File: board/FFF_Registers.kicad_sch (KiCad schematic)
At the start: 19 parts, among them U1 74F573, U14 74F32, U18 74F04, U2 74F541, U47 74F573, U48 74F541, U49 74F573, U50 74F541, U51 74F32, U52 74F04

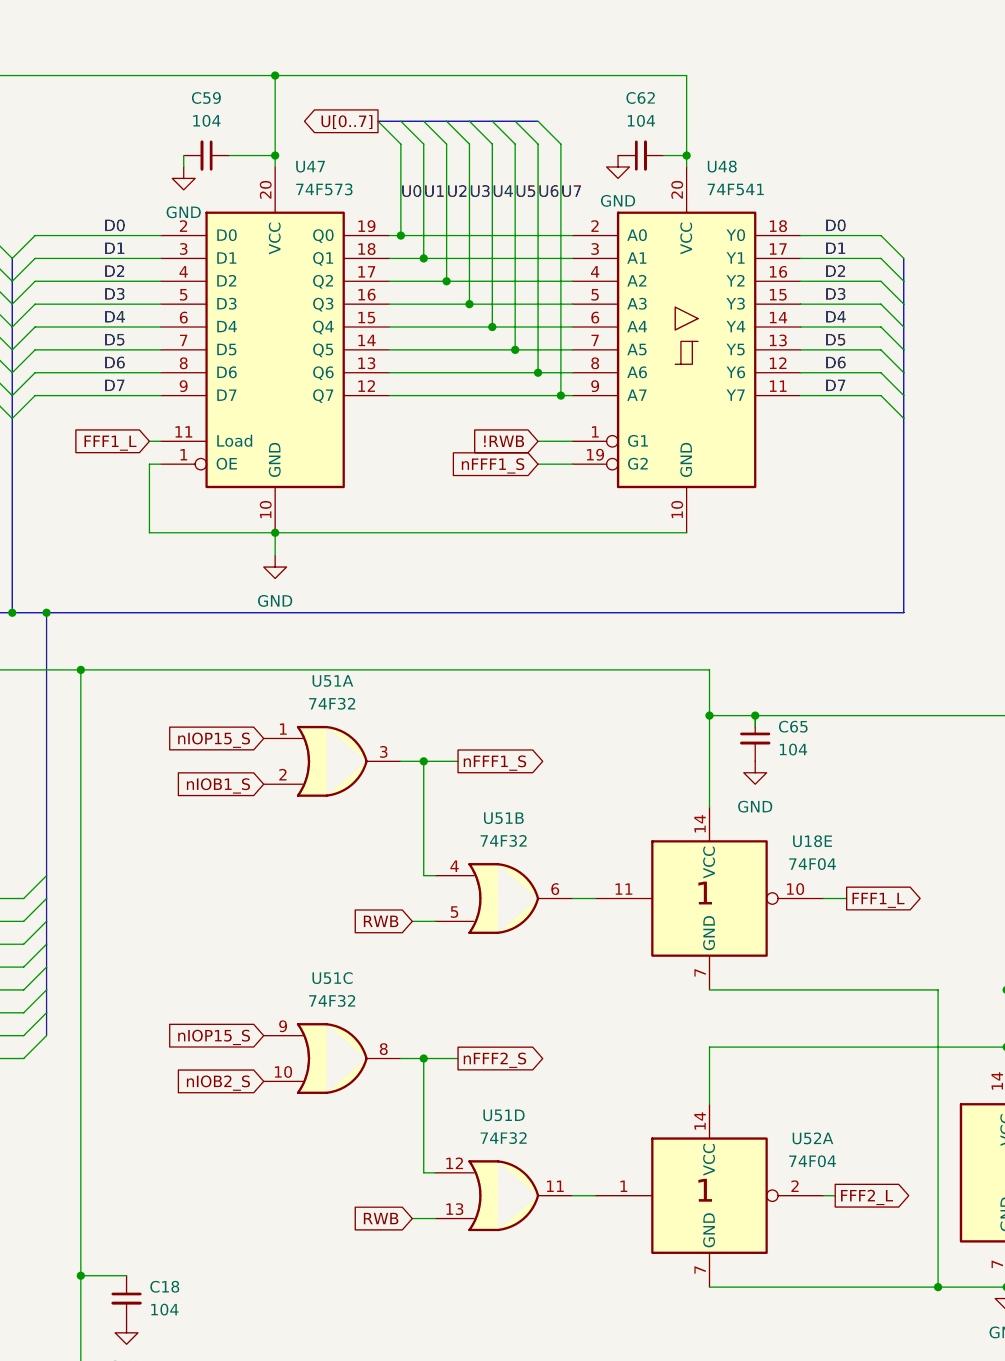
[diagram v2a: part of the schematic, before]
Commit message: Fixing nBROMD routing, removing unnecessary 7404, and minor other cleanup.
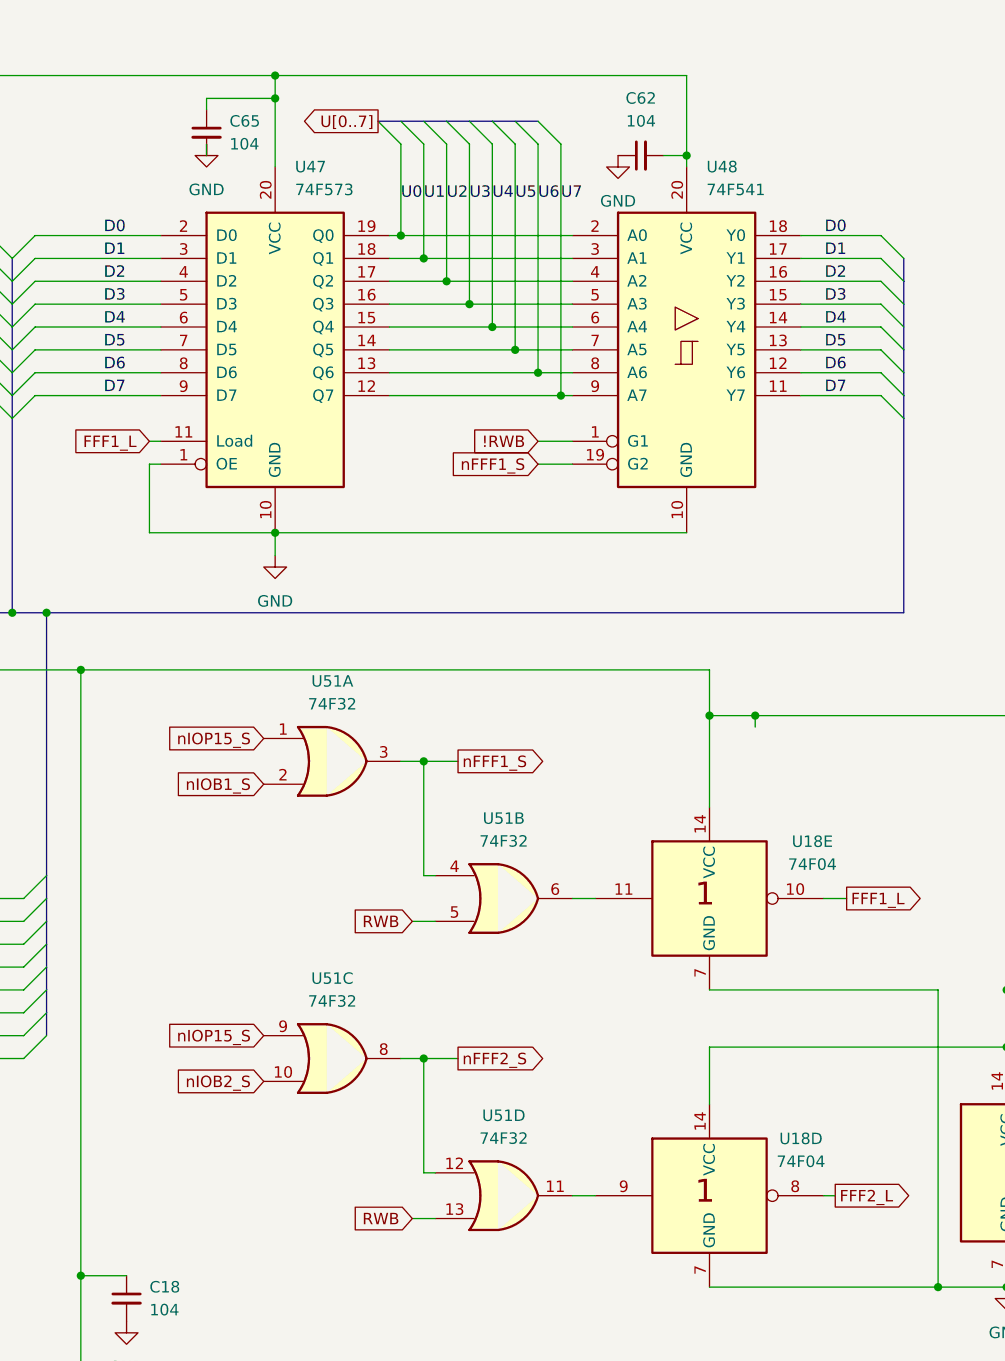
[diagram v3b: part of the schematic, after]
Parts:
- removed C59: 104, Capacitor_THT:C_Disc_D5.0mm_W2.5mm_P5.00mm, symbol Device:C_Small
- removed U52: 74F04, Package_DIP:DIP-14_W7.62mm_Socket_LongPads, symbol 74xx_IEEE:7404
- added unit 4 of U18
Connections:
- net +5V: now also U18.14 (VCC)
- net FFF2_L: now also U18.8
- net GND: now also U18.7 (GND)
- net at U51.11: now also U18.9
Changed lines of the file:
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@@
 	)
 	(junction
+		(at 156.21 26.67)
+		(diameter 0)
+		(color 0 0 0 0)
+	)
+	(junction
 		(at 78.74 49.53)
 		(diameter 0)
@@
 	)
 	(junction
-		(at 156.21 33.02)
-		(diameter 0)
-		(color 0 0 0 0)
-	)
-	(junction
 		(at 209.55 95.25)
 		(diameter 0)
@@
 	(wire
 		(pts
+			(xy 148.59 31.75) (xy 148.59 33.02)
+		)
+		(stroke
+			(width 0)
+			(type default)
+		)
+	)
+	(wire
+		(pts
 			(xy 115.57 52.07) (xy 124.46 52.07)
 		)
@@
 	(wire
 		(pts
-			(xy 151.13 33.02) (xy 156.21 33.02)
-		)
-		(stroke
-			(width 0)
-			(type default)
-		)
-	)
-	(wire
-		(pts
 			(xy 73.66 130.81) (xy 90.17 130.81)
 		)
@@
 	(wire
 		(pts
-			(xy 156.21 24.13) (xy 156.21 33.02)
+			(xy 156.21 24.13) (xy 156.21 26.67)
 		)
 		(stroke
@@
 	(wire
 		(pts
+			(xy 148.59 27.94) (xy 148.59 26.67)
+		)
+		(stroke
+			(width 0)
+			(type default)
+		)
+	)
+	(wire
+		(pts
 			(xy 34.29 49.53) (xy 44.45 49.53)
 		)
@@
 	(wire
 		(pts
-			(xy 146.05 33.02) (xy 146.05 34.29)
-		)
-		(stroke
-			(width 0)
-			(type default)
-		)
-	)
-	(wire
-		(pts
 			(xy 129.54 44.45) (xy 143.51 44.45)
 		)
@@
 	(wire
 		(pts
-			(xy 156.21 33.02) (xy 156.21 34.29)
-		)
-		(stroke
-			(width 0)
-			(type default)
-		)
-	)
-	(wire
-		(pts
 			(xy 129.54 57.15) (xy 143.51 57.15)
 		)
@@
 	(wire
 		(pts
+			(xy 156.21 26.67) (xy 156.21 34.29)
+		)
+		(stroke
+			(width 0)
+			(type default)
+		)
+	)
+	(wire
+		(pts
 			(xy 229.87 158.75) (xy 237.49 158.75)
 		)
@@
 	(wire
 		(pts
+			(xy 148.59 26.67) (xy 156.21 26.67)
+		)
+		(stroke
+			(width 0)
+			(type default)
+		)
+	)
+	(wire
+		(pts
 			(xy 82.55 104.14) (xy 82.55 123.19)
 		)
@@
 	)
 	(symbol
-		(lib_id "power:GND")
-		(at 209.55 100.33 0)
-		(unit 1)
-		(exclude_from_sim no)
-		(in_bom yes)
-		(on_board yes)
-		(dnp no)
-		(fields_autoplaced yes)
-		(property "Reference" "#PWR088"
-			(at 209.55 106.68 0)
-			(effects
-				(font
-					(size 1.27 1.27)
-				)
-				(hide yes)
-			)
-		)
-		(property "Value" "GND"
-			(at 209.55 105.41 0)
-			(effects
-				(font
-					(size 1.27 1.27)
-				)
-			)
-		)
-		(property "Footprint" ""
-			(at 209.55 100.33 0)
-			(effects
-				(font
-					(size 1.27 1.27)
-				)
-				(hide yes)
-			)
-		)
-		(property "Datasheet" ""
-			(at 209.55 100.33 0)
-			(effects
-				(font
-					(size 1.27 1.27)
-				)
-				(hide yes)
-			)
-		)
-		(property "Description" "Power symbol creates a global label with name \"GND\" , ground"
-			(at 209.55 100.33 0)
-			(effects
-				(font
-					(size 1.27 1.27)
-				)
-				(hide yes)
-			)
-		)
-		(pin "1"
-		)
-		(instances
-			(project "hydra-16"
-				(path "/ef29fc71-3fec-48b5-8a1a-46bee537a98c/9c3f9893-75ea-4823-afb7-35bb324a2c9f"
-					(reference "#PWR088")
-					(unit 1)
-				)
-			)
-		)
-	)
-	(symbol
 		(lib_id "power:+5V")
 		(at 102.87 24.13 0)
@@
 	(symbol
 		(lib_id "power:GND")
-		(at 146.05 34.29 0)
+		(at 148.59 31.75 0)
 		(unit 1)
 		(exclude_from_sim no)
@@
 		(fields_autoplaced yes)
 		(property "Reference" "#PWR081"
-			(at 146.05 40.64 0)
+			(at 148.59 38.1 0)
 			(effects
 				(font
@@
 		)
 		(property "Value" "GND"
-			(at 146.05 39.37 0)
+			(at 148.59 36.83 0)
 			(effects
 				(font
@@
 		)
 		(property "Footprint" ""
-			(at 146.05 34.29 0)
+			(at 148.59 31.75 0)
 			(effects
 				(font
@@
 		)
 		(property "Datasheet" ""
-			(at 146.05 34.29 0)
+			(at 148.59 31.75 0)
 			(effects
 				(font
@@
 		)
 		(property "Description" "Power symbol creates a global label with name \"GND\" , ground"
-			(at 146.05 34.29 0)
+			(at 148.59 31.75 0)
 			(effects
 				(font
@@
 	(symbol
 		(lib_id "Device:C_Small")
-		(at 209.55 97.79 0)
-		(unit 1)
-		(exclude_from_sim no)
-		(in_bom yes)
-		(on_board yes)
-		(dnp no)
-		(fields_autoplaced yes)
-		(property "Reference" "C65"
-			(at 212.09 96.5262 0)
-			(effects
-				(font
-					(size 1.27 1.27)
-				)
-				(justify left)
-			)
-		)
-		(property "Value" "104"
-			(at 212.09 99.0662 0)
-			(effects
-				(font
-					(size 1.27 1.27)
-				)
-				(justify left)
-			)
-		)
-		(property "Footprint" "Capacitor_THT:C_Disc_D5.0mm_W2.5mm_P5.00mm"
-			(at 209.55 97.79 0)
-			(effects
-				(font
-					(size 1.27 1.27)
-				)
-				(hide yes)
-			)
-		)
-		(property "Datasheet" "~"
-			(at 209.55 97.79 0)
-			(effects
-				(font
-					(size 1.27 1.27)
-				)
-				(hide yes)
-			)
-		)
-		(property "Description" "Unpolarized capacitor, small symbol"
-			(at 209.55 97.79 0)
-			(effects
-				(font
-					(size 1.27 1.27)
-				)
-				(hide yes)
-			)
-		)
-		(pin "1"
-		)
-		(pin "2"
-		)
-		(instances
-			(project "hydra-16"
-				(path "/ef29fc71-3fec-48b5-8a1a-46bee537a98c/9c3f9893-75ea-4823-afb7-35bb324a2c9f"
-					(reference "C65")
-					(unit 1)
-				)
-			)
-		)
-	)
-	(symbol
-		(lib_id "Device:C_Small")
 		(at 241.3 128.27 0)
 		(unit 1)
@@
 	(symbol
 		(lib_id "Device:C_Small")
-		(at 148.59 33.02 270)
+		(at 148.59 30.48 0)
 		(unit 1)
 		(exclude_from_sim no)
@@
 		(dnp no)
 		(fields_autoplaced yes)
-		(property "Reference" "C59"
-			(at 148.5836 26.67 90)
+		(property "Reference" "C65"
+			(at 151.13 29.2162 0)
 			(effects
 				(font
 					(size 1.27 1.27)
 				)
+				(justify left)
 			)
 		)
 		(property "Value" "104"
-			(at 148.5836 29.21 90)
+			(at 151.13 31.7562 0)
 			(effects
 				(font
 					(size 1.27 1.27)
 				)
+				(justify left)
 			)
 		)
 		(property "Footprint" "Capacitor_THT:C_Disc_D5.0mm_W2.5mm_P5.00mm"
-			(at 148.59 33.02 0)
+			(at 148.59 30.48 0)
 			(effects
 				(font
@@
 		)
 		(property "Datasheet" "~"
-			(at 148.59 33.02 0)
+			(at 148.59 30.48 0)
 			(effects
 				(font
@@
 		)
 		(property "Description" "Unpolarized capacitor, small symbol"
-			(at 148.59 33.02 0)
+			(at 148.59 30.48 0)
 			(effects
 				(font
@@
 			(project "hydra-16"
 				(path "/ef29fc71-3fec-48b5-8a1a-46bee537a98c/9c3f9893-75ea-4823-afb7-35bb324a2c9f"
-					(reference "C59")
+					(reference "C65")
 					(unit 1)
 				)
@@
 		(lib_id "74xx_IEEE:7404")
 		(at 204.47 148.59 0)
-		(unit 1)
+		(unit 4)
 		(exclude_from_sim no)
 		(in_bom yes)
@@
 		(dnp no)
 		(fields_autoplaced yes)
-		(property "Reference" "U52"
-			(at 215.9 142.2714 0)
+		(property "Reference" "U18"
+			(at 214.63 142.2714 0)
 			(effects
 				(font
@@
 		)
 		(property "Value" "74F04"
-			(at 215.9 144.8114 0)
+			(at 214.63 144.8114 0)
 			(effects
 				(font
@@
 			(project "hydra-16"
 				(path "/ef29fc71-3fec-48b5-8a1a-46bee537a98c/9c3f9893-75ea-4823-afb7-35bb324a2c9f"
-					(reference "U52")
-					(unit 1)
+					(reference "U18")
+					(unit 4)
 				)
 			)

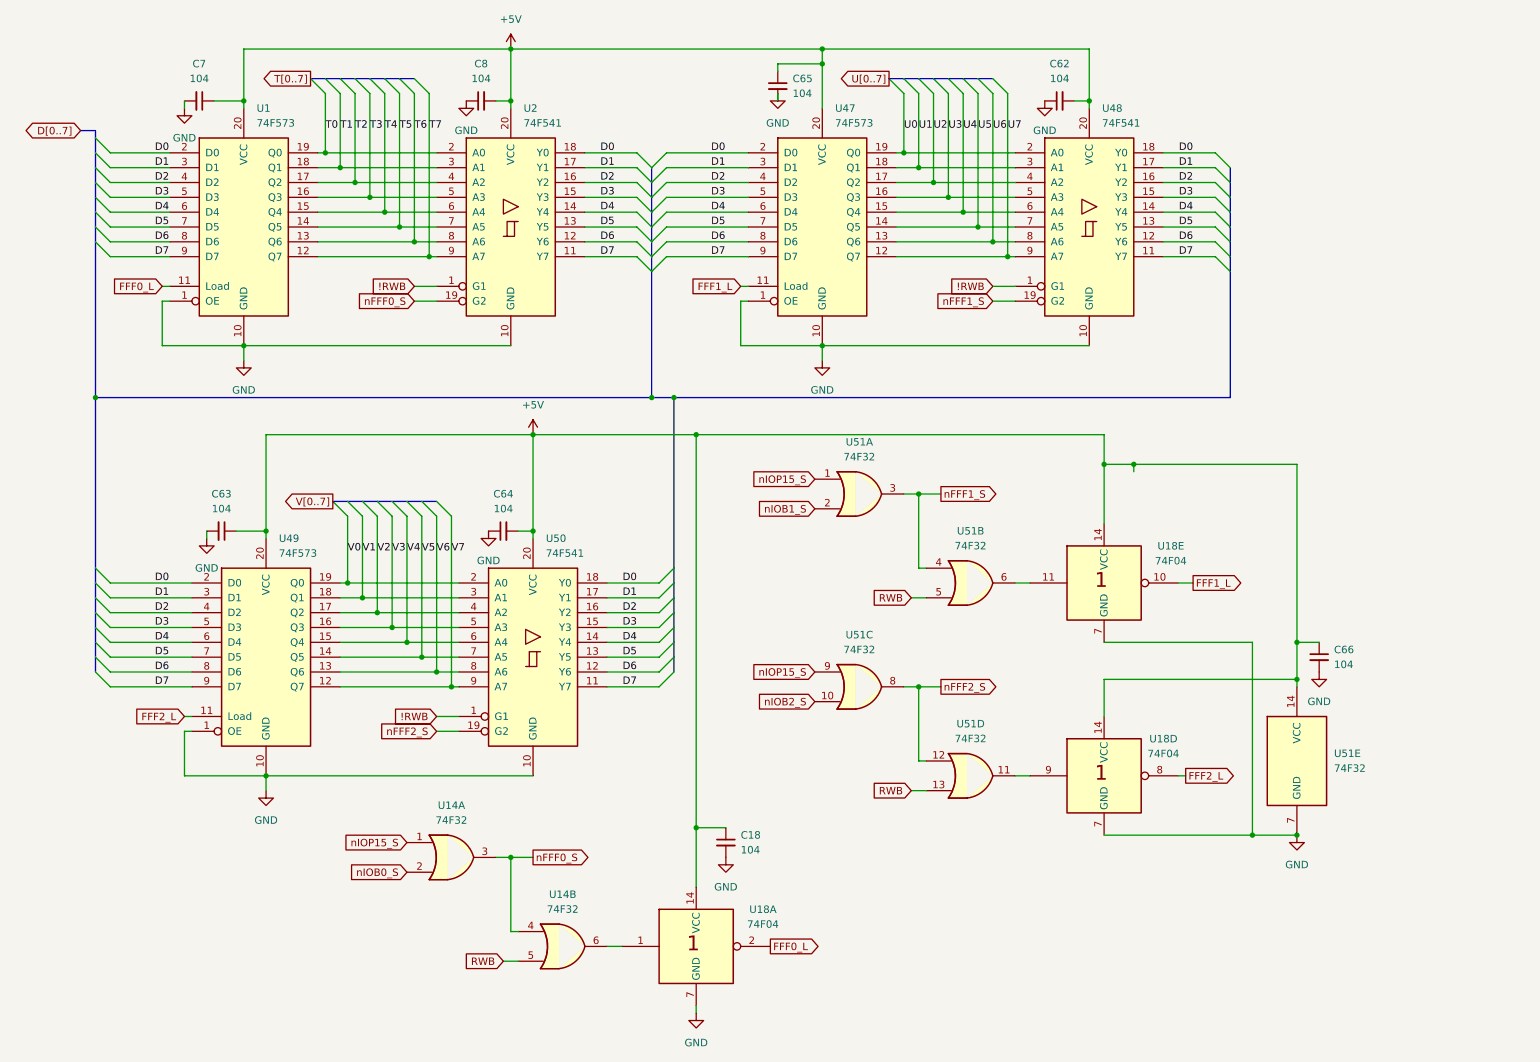
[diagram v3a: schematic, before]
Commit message: Added VIA port A header and voltage protection diode package socket. Updated logic.
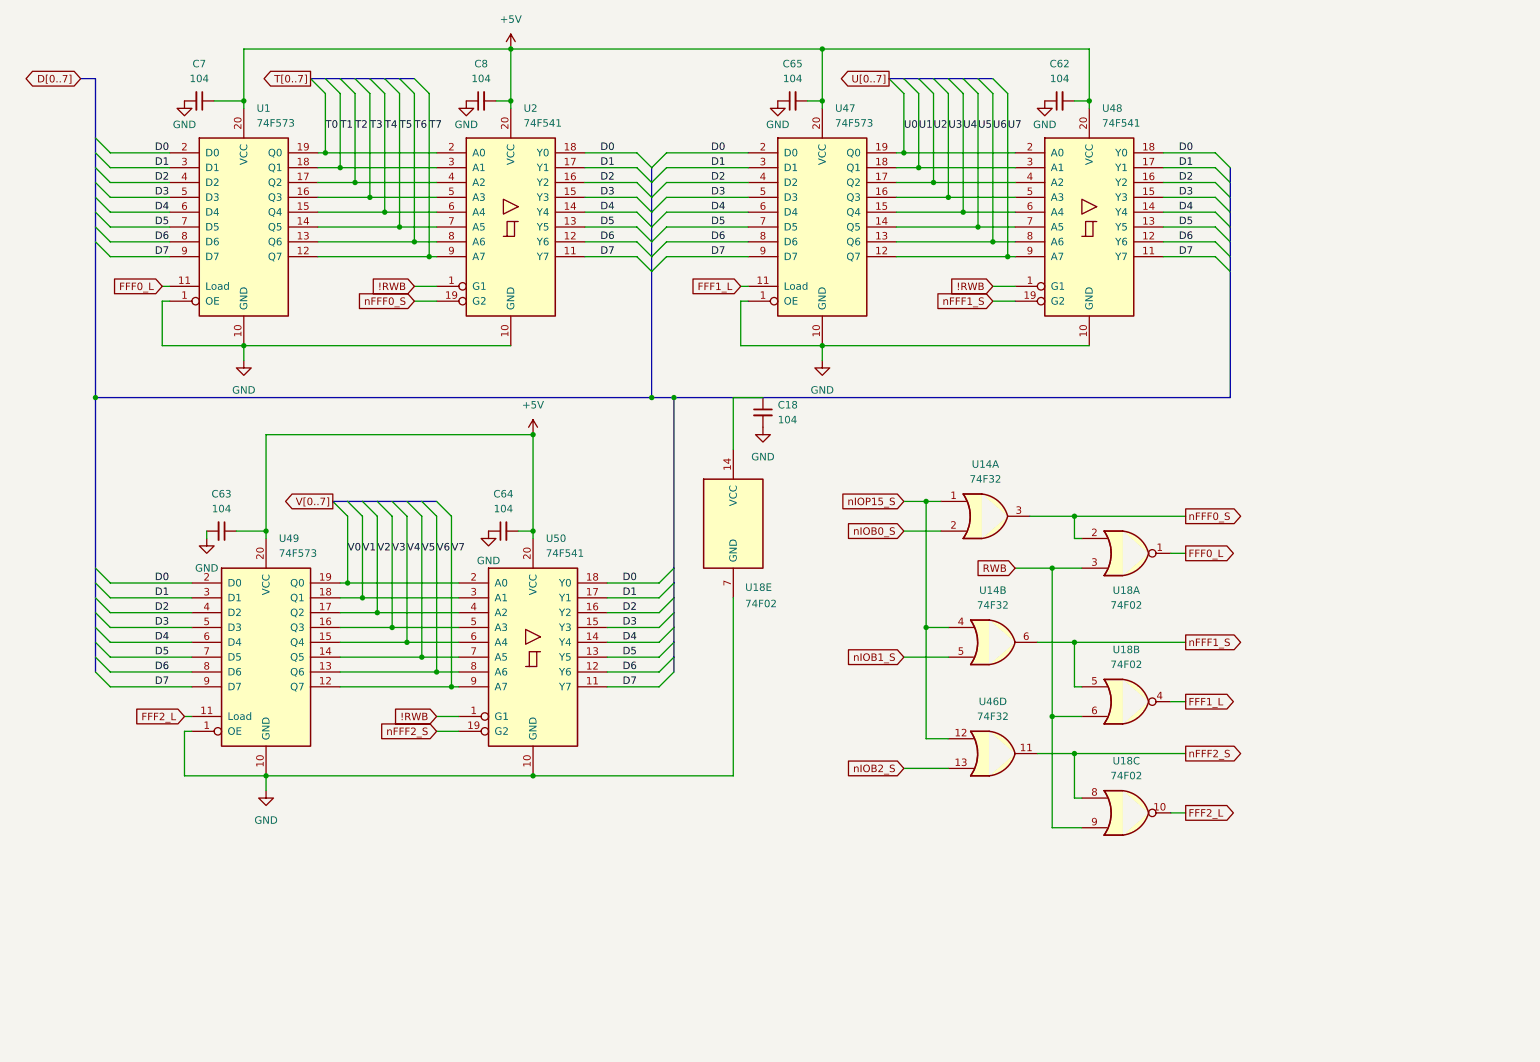
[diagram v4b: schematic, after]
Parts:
- removed C66: 104, Capacitor_THT:C_Disc_D5.0mm_W2.5mm_P5.00mm, symbol Device:C_Small
- removed U18: 74F04, Package_DIP:DIP-14_W7.62mm_Socket_LongPads, symbol 74xx_IEEE:7404
- removed U51: 74F32, Package_DIP:DIP-14_W7.62mm_Socket_LongPads, symbol 74xx:74LS32
- added U18: 74F02, Package_DIP:DIP-14_W7.62mm_Socket_LongPads, symbol 74xx:7402
- added U46: 74F32, Package_DIP:DIP-14_W7.62mm_Socket_LongPads, symbol 74xx:74LS32
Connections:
- net +5V: now also C65.2; no longer C18.1, C65.1
- net FFF0_L: now also U18.1
- net FFF1_L: now also U18.4
- net FFF2_L: now also U18.10
- net GND: now also C65.1, U18.7 (GND); no longer C65.2
- net RWB: now also U18.3, U18.6, U18.9; no longer U14.5
- net nFFF0_S: now also U18.2; no longer U14.4
- net nFFF1_S: now also U14.6, U18.5
- net nFFF2_S: now also U18.8, U46.11
- net nIOB1_S: now also U14.5
- net nIOB2_S: now also U46.13
- net nIOP15_S: now also U14.4, U46.12
- new net: C18.1, U18.14 (VCC)
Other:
- moved on the sheet: C65, U14A
